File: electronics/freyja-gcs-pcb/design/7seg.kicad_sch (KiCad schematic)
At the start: 21 parts, among them Q24 AO4459, Q25 AO4459, U13 74HC595, U14 74HC595

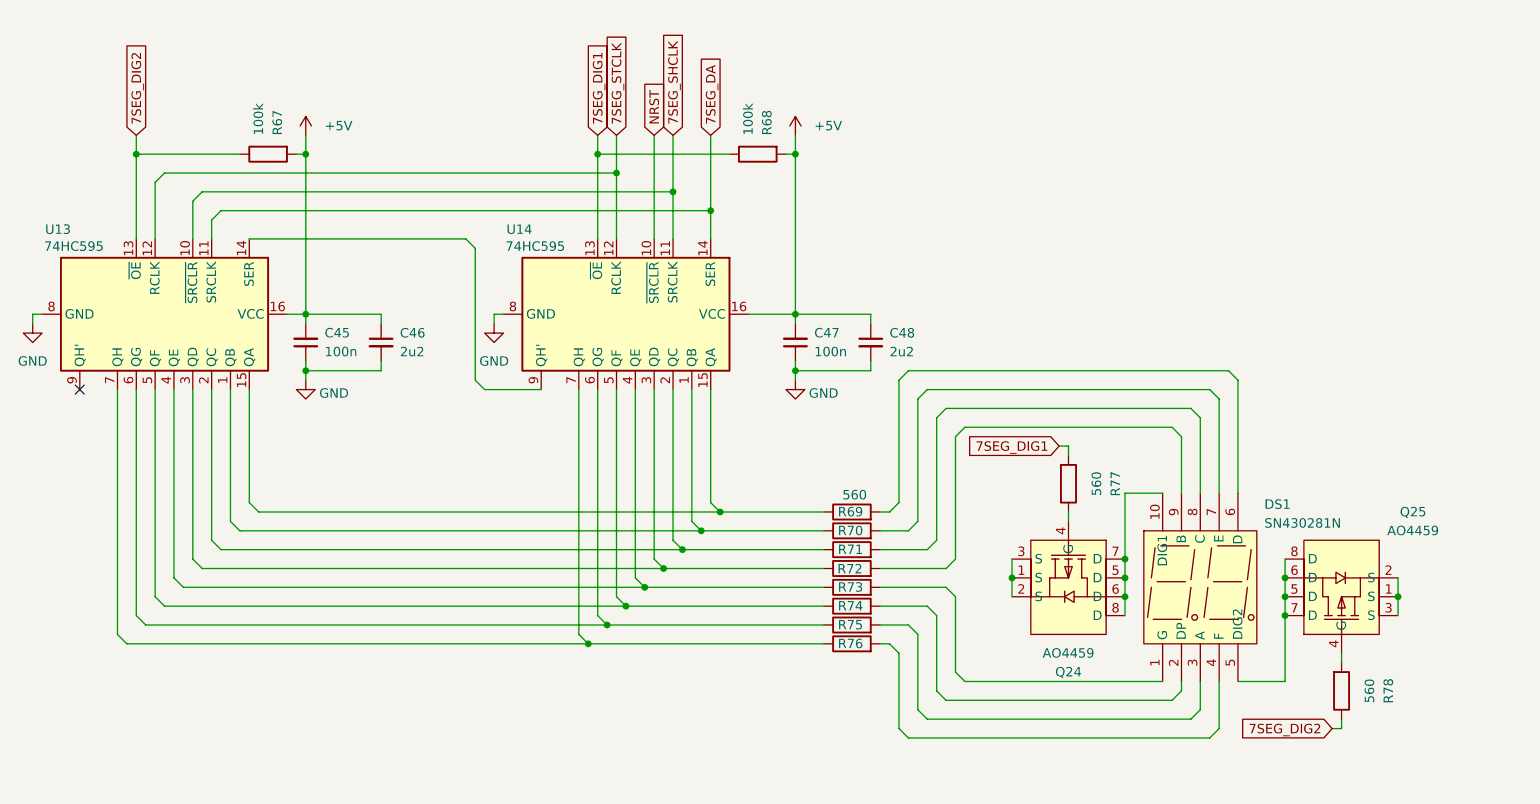
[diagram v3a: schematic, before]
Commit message: Updated PCB layout and grouped components
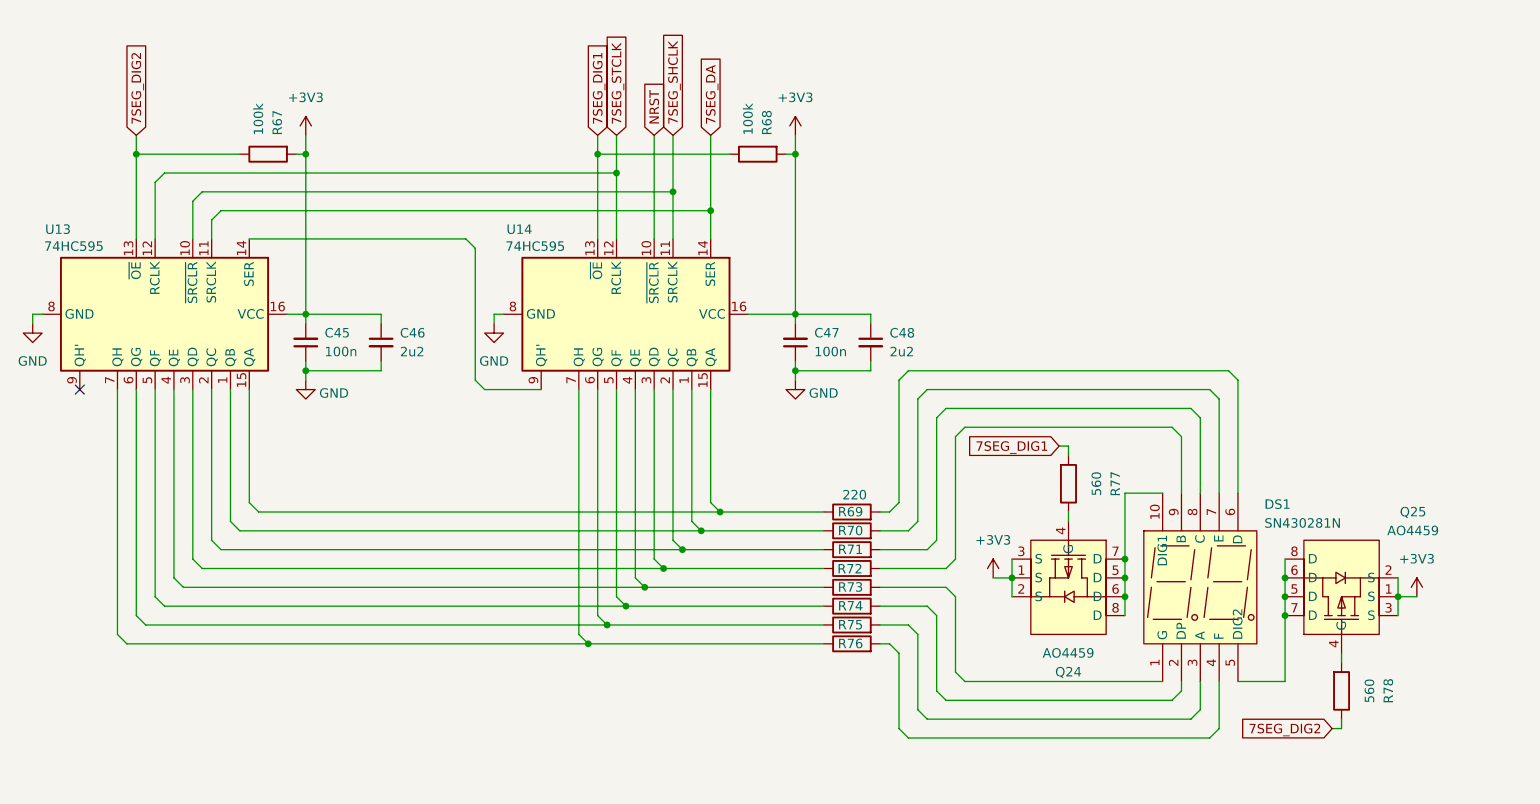
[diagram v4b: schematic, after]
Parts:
- R69, R70, R71, R72, R73, R74, R75, R76: value 560 -> 220
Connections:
- net +5V is gone; now on net +3V3: C45.2, C46.1, C47.2, C48.1, R67.2, R68.2, U13.16 (VCC), U14.16 (VCC)
- net +3V3: now reaches Q24.1 (S), Q24.2 (S), Q24.3 (S)
- net +3V3: now also Q25.1 (S), Q25.2 (S), Q25.3 (S)
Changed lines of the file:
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@@
+	(wire
+		(pts
+			(xy 245.11 120.65) (xy 247.65 120.65)
+		)
+		(stroke
+			(width 0)
+			(type default)
+		)
+	)
 	(wire
 		(pts
@@
 		(pts
 			(xy 245.11 118.11) (xy 245.11 120.65)
+		)
+		(stroke
+			(width 0)
+			(type default)
+		)
+	)
+	(wire
+		(pts
+			(xy 190.5 118.11) (xy 193.04 118.11)
 		)
 		(stroke
@@
 			)
 		)
-		(property "Value" "560"
+		(property "Value" "220"
 			(at 172.72 149.606 0)
 			(effects
@@
 	)
 	(symbol
-		(lib_id "power:+5V")
-		(at 163.83 58.42 0)
-		(unit 1)
-		(exclude_from_sim no)
-		(in_bom yes)
-		(on_board yes)
-		(dnp no)
-		(fields_autoplaced yes)
-		(property "Reference" "#PWR0116"
-			(at 163.83 62.23 0)
-			(effects
-				(font
-					(size 1.27 1.27)
-				)
-				(hide yes)
-			)
-		)
-		(property "Value" "+5V"
-			(at 166.37 57.1499 0)
-			(effects
-				(font
-					(size 1.27 1.27)
-				)
-				(justify left)
-			)
-		)
-		(property "Footprint" ""
-			(at 163.83 58.42 0)
-			(effects
-				(font
-					(size 1.27 1.27)
-				)
-				(hide yes)
-			)
-		)
-		(property "Datasheet" ""
-			(at 163.83 58.42 0)
-			(effects
-				(font
-					(size 1.27 1.27)
-				)
-				(hide yes)
-			)
-		)
-		(property "Description" "Power symbol creates a global label with name \"+5V\""
-			(at 163.83 58.42 0)
-			(effects
-				(font
-					(size 1.27 1.27)
-				)
-				(hide yes)
-			)
-		)
-		(pin "1"
-		)
-		(instances
-			(project "freyja-gcs-pcb"
-				(path "/c292fa04-82ad-49e9-a9d8-422554d1d11d/824ebaf0-8cb2-47d2-898f-7e11886db031"
-					(reference "#PWR0116")
-					(unit 1)
-				)
-			)
-		)
-	)
-	(symbol
 		(lib_id "Device:C_Small")
 		(at 107.95 86.36 0)
@@
 			)
 		)
-		(property "Value" "560"
+		(property "Value" "220"
 			(at 172.72 157.734 0)
 			(effects
@@
 	)
 	(symbol
+		(lib_id "power:+3V3")
+		(at 97.79 58.42 0)
+		(unit 1)
+		(exclude_from_sim no)
+		(in_bom yes)
+		(on_board yes)
+		(dnp no)
+		(fields_autoplaced yes)
+		(property "Reference" "#PWR0113"
+			(at 97.79 62.23 0)
+			(effects
+				(font
+					(size 1.27 1.27)
+				)
+				(hide yes)
+			)
+		)
+		(property "Value" "+3V3"
+			(at 97.79 53.34 0)
+			(effects
+				(font
+					(size 1.27 1.27)
+				)
+			)
+		)
+		(property "Footprint" ""
+			(at 97.79 58.42 0)
+			(effects
+				(font
+					(size 1.27 1.27)
+				)
+				(hide yes)
+			)
+		)
+		(property "Datasheet" ""
+			(at 97.79 58.42 0)
+			(effects
+				(font
+					(size 1.27 1.27)
+				)
+				(hide yes)
+			)
+		)
+		(property "Description" "Power symbol creates a global label with name \"+3V3\""
+			(at 97.79 58.42 0)
+			(effects
+				(font
+					(size 1.27 1.27)
+				)
+				(hide yes)
+			)
+		)
+		(pin "1"
+		)
+		(instances
+			(project ""
+				(path "/c292fa04-82ad-49e9-a9d8-422554d1d11d/824ebaf0-8cb2-47d2-898f-7e11886db031"
+					(reference "#PWR0113")
+					(unit 1)
+				)
+			)
+		)
+	)
+	(symbol
 		(lib_id "Device:C_Small")
 		(at 173.99 86.36 0)
@@
 	)
 	(symbol
-		(lib_id "power:+5V")
-		(at 97.79 58.42 0)
+		(lib_id "power:+3V3")
+		(at 163.83 58.42 0)
 		(unit 1)
 		(exclude_from_sim no)
@@
 		(dnp no)
 		(fields_autoplaced yes)
-		(property "Reference" "#PWR0113"
-			(at 97.79 62.23 0)
-			(effects
-				(font
-					(size 1.27 1.27)
-				)
-				(hide yes)
-			)
-		)
-		(property "Value" "+5V"
-			(at 100.33 57.1499 0)
-			(effects
-				(font
-					(size 1.27 1.27)
-				)
-				(justify left)
+		(property "Reference" "#PWR0116"
+			(at 163.83 62.23 0)
+			(effects
+				(font
+					(size 1.27 1.27)
+				)
+				(hide yes)
+			)
+		)
+		(property "Value" "+3V3"
+			(at 163.83 53.34 0)
+			(effects
+				(font
+					(size 1.27 1.27)
+				)
 			)
 		)
 		(property "Footprint" ""
-			(at 97.79 58.42 0)
+			(at 163.83 58.42 0)
 			(effects
 				(font
@@
 		)
 		(property "Datasheet" ""
-			(at 97.79 58.42 0)
-			(effects
-				(font
-					(size 1.27 1.27)
-				)
-				(hide yes)
-			)
-		)
-		(property "Description" "Power symbol creates a global label with name \"+5V\""
-			(at 97.79 58.42 0)
+			(at 163.83 58.42 0)
+			(effects
+				(font
+					(size 1.27 1.27)
+				)
+				(hide yes)
+			)
+		)
+		(property "Description" "Power symbol creates a global label with name \"+3V3\""
+			(at 163.83 58.42 0)
 			(effects
 				(font
@@
 		)
 		(instances
-			(project "freyja-gcs-pcb"
+			(project ""
 				(path "/c292fa04-82ad-49e9-a9d8-422554d1d11d/824ebaf0-8cb2-47d2-898f-7e11886db031"
-					(reference "#PWR0113")
+					(reference "#PWR0116")
 					(unit 1)
 				)
@@
 			)
 		)
-		(property "Value" "560"
+		(property "Value" "220"
 			(at 173.482 106.934 90)
 			(effects
@@
 			)
 		)
-		(property "Value" "560"
+		(property "Value" "220"
 			(at 172.72 153.67 0)
 			(effects
@@
 			)
 		)
-		(property "Value" "560"
+		(property "Value" "220"
 			(at 172.72 161.798 0)
 			(effects
@@
 			)
 		)
-		(property "Value" "560"
+		(property "Value" "220"
 			(at 172.6502 145.6195 0)
 			(effects
@@
 			)
 		)
-		(property "Value" "560"
+		(property "Value" "220"
 			(at 172.72 141.478 0)
 			(effects
@@
 			)
 		)
-		(property "Value" "560"
+		(property "Value" "220"
 			(at 172.6502 137.2375 0)
 			(effects
@@
 				(path "/c292fa04-82ad-49e9-a9d8-422554d1d11d/824ebaf0-8cb2-47d2-898f-7e11886db031"
 					(reference "R70")
+					(unit 1)
+				)
+			)
+		)
+	)
+	(symbol
+		(lib_id "power:+3V3")
+		(at 247.65 120.65 0)
+		(unit 1)
+		(exclude_from_sim no)
+		(in_bom yes)
+		(on_board yes)
+		(dnp no)
+		(fields_autoplaced yes)
+		(property "Reference" "#PWR0119"
+			(at 247.65 124.46 0)
+			(effects
+				(font
+					(size 1.27 1.27)
+				)
+				(hide yes)
+			)
+		)
+		(property "Value" "+3V3"
+			(at 247.65 115.57 0)
+			(effects
+				(font
+					(size 1.27 1.27)
+				)
+			)
+		)
+		(property "Footprint" ""
+			(at 247.65 120.65 0)
+			(effects
+				(font
+					(size 1.27 1.27)
+				)
+				(hide yes)
+			)
+		)
+		(property "Datasheet" ""
+			(at 247.65 120.65 0)
+			(effects
+				(font
+					(size 1.27 1.27)
+				)
+				(hide yes)
+			)
+		)
+		(property "Description" "Power symbol creates a global label with name \"+3V3\""
+			(at 247.65 120.65 0)
+			(effects
+				(font
+					(size 1.27 1.27)
+				)
+				(hide yes)
+			)
+		)
+		(pin "1"
+		)
+		(instances
+			(project "freyja-gcs-pcb"
+				(path "/c292fa04-82ad-49e9-a9d8-422554d1d11d/824ebaf0-8cb2-47d2-898f-7e11886db031"
+					(reference "#PWR0119")
 					(unit 1)
 				)
@@
 					(unit 1)
 				)
+			)
+		)
+	)
+	(symbol
+		(lib_id "power:+3V3")
+		(at 190.5 118.11 0)
+		(unit 1)
+		(exclude_from_sim no)
+		(in_bom yes)
+		(on_board yes)
+		(dnp no)
+		(fields_autoplaced yes)
+		(property "Reference" "#PWR0118"
+			(at 190.5 121.92 0)
+			(effects
+				(font
+					(size 1.27 1.27)
+				)
+				(hide yes)
+			)
+		)
+		(property "Value" "+3V3"
+			(at 190.5 113.03 0)
+			(effects
+				(font
+					(size 1.27 1.27)
+				)
+			)
+		)
+		(property "Footprint" ""
+			(at 190.5 118.11 0)
+			(effects
+				(font
+					(size 1.27 1.27)
+				)
+				(hide yes)
+			)
+		)
+		(property "Datasheet" ""
+			(at 190.5 118.11 0)
+			(effects
+				(font
+					(size 1.27 1.27)
+				)
+				(hide yes)
+			)
+		)
+		(property "Description" "Power symbol creates a global label with name \"+3V3\""
+			(at 190.5 118.11 0)
+			(effects
+				(font
+					(size 1.27 1.27)
+				)
+				(hide yes)
+			)
+		)
+		(pin "1"
+		)
+		(instances
+			(project "freyja-gcs-pcb"
+				(path "/c292fa04-82ad-49e9-a9d8-422554d1d11d/824ebaf0-8cb2-47d2-898f-7e11886db031"
+					(reference "#PWR0118")
+					(unit 1)
+				)

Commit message: btn routing wip
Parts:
- added Q27: NPN, EasyEDA:SOT-416_L1.6-W0.8-P1.00-LS1.6-BR, symbol EasyEDA:DTC043ZEBTL
- R78: value 560 -> 10k; LCSC Part C23204 -> C98220
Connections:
- net +3V3: now also R78.1
- net 7SEG_DA: no longer U13.11 (SRCLK)
- net 7SEG_DIG1: no longer R77.2
- net 7SEG_DIG2: no longer R78.1
- net 7SEG_SHCLK: now also U13.11 (SRCLK); no longer U13.10 (~{SRCLR})
- net GND: now also Q27.2 (E)
- net NRST: now also U13.10 (~{SRCLR})
- net at Q25.4 (G), R78.2: now also Q27.3 (C)
- new net 7SEG_PWM: Q27.1 (B), R77.2
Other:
- moved on the sheet: Q25

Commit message: btn routing wip
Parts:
- removed Q27: NPN, EasyEDA:SOT-416_L1.6-W0.8-P1.00-LS1.6-BR, symbol EasyEDA:DTC043ZEBTL
- R78: value 10k -> 560; LCSC Part C98220 -> C23204
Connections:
- net 7SEG_PWM is gone; now on net 7SEG_DIG1: R77.2
- net +3V3: no longer R78.1
- net 7SEG_DIG2: now also R78.1

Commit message: change to available parts
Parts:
- R69, R70, R71, R72, R73, R74, R75, R76: LCSC Part C23204 -> C22962
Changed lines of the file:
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@@
 			)
 		)
-		(property "LCSC Part" "C23204"
+		(property "LCSC Part" "C22962"
 			(at 171.45 119.38 90)
 			(effects
@@
 			)
 		)
-		(property "LCSC Part" "C23204"
+		(property "LCSC Part" "C22962"
 			(at 171.45 124.46 90)
 			(effects
@@
 			)
 		)
-		(property "LCSC Part" "C23204"
+		(property "LCSC Part" "C22962"
 			(at 171.45 109.22 90)
 			(effects
@@
 			)
 		)
-		(property "LCSC Part" "C23204"
+		(property "LCSC Part" "C22962"
 			(at 171.45 121.92 90)
 			(effects
@@
 			)
 		)
-		(property "LCSC Part" "C23204"
+		(property "LCSC Part" "C22962"
 			(at 171.45 127 90)
 			(effects
@@
 			)
 		)
-		(property "LCSC Part" "C23204"
+		(property "LCSC Part" "C22962"
 			(at 171.45 116.84 90)
 			(effects
@@
 			)
 		)
-		(property "LCSC Part" "C23204"
+		(property "LCSC Part" "C22962"
 			(at 171.45 114.3 90)
 			(effects
@@
 			)
 		)
-		(property "LCSC Part" "C23204"
+		(property "LCSC Part" "C22962"
 			(at 171.45 111.76 90)
 			(effects
